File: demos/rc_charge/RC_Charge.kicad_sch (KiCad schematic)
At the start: 3 parts

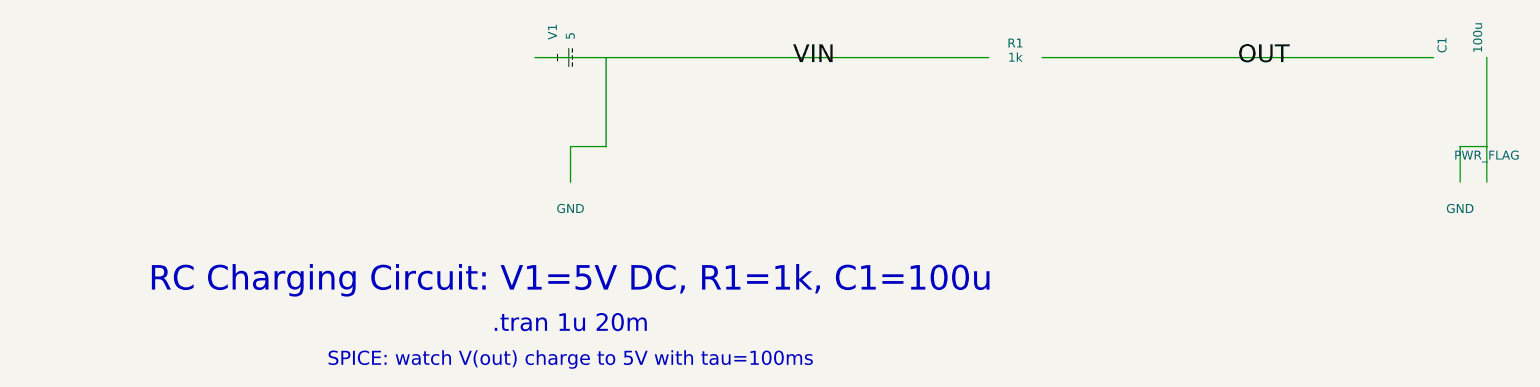
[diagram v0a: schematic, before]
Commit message: feat: Integrate SPICE simulation support into KiCad's GUI
- Added `handleSimulate` method in `api_handler_sch` to manage SPICE simulations.
- Implemented a new `Simulate` command in the API to trigger simulations from the schematic.
- Enhanced `NGSPICE` integration to handle optional symbols for compatibility with various builds.
- Introduced `kicad_sch_simulate_gui` function in Python client to run simulations and display results in KiCad's GUI.
- Updated tests to include simulation functionality and validate the integration.
- Documented changes and usage instructions for the new simulation features.
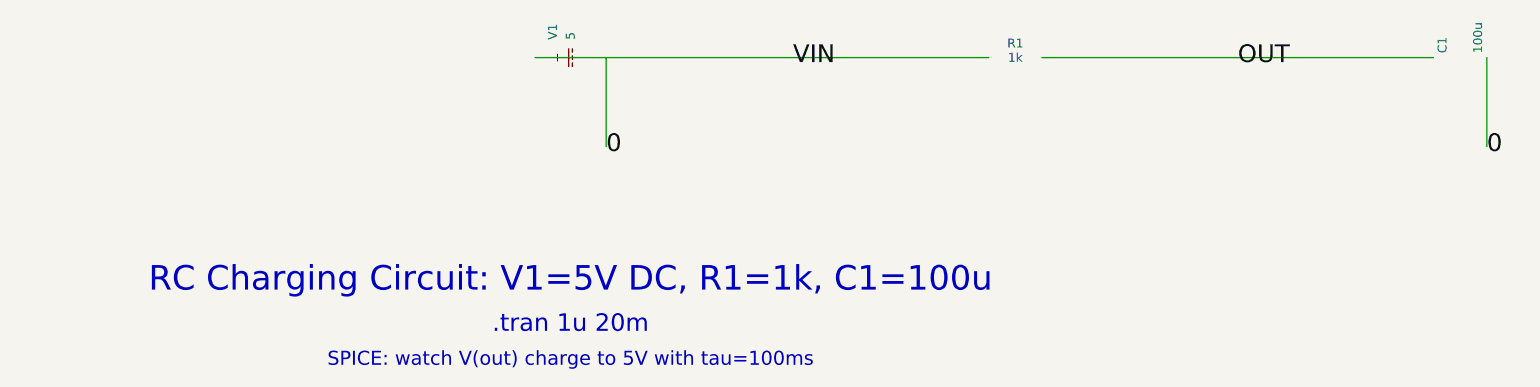
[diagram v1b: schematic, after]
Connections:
- net GND renamed 0

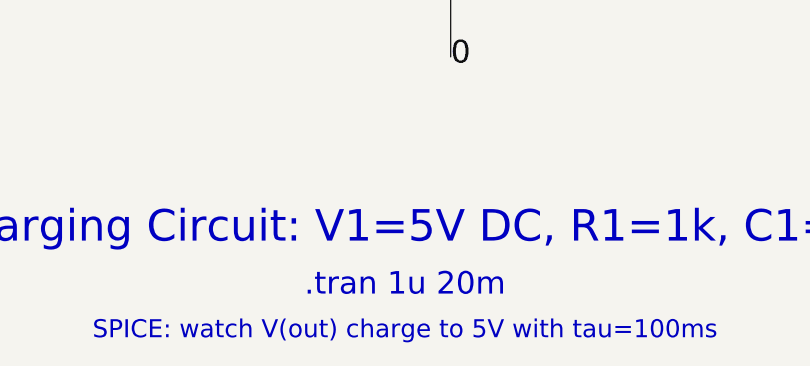
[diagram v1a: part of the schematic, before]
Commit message: feat: 增加信号自动显示功能，优化 SPICE 仿真结果分析
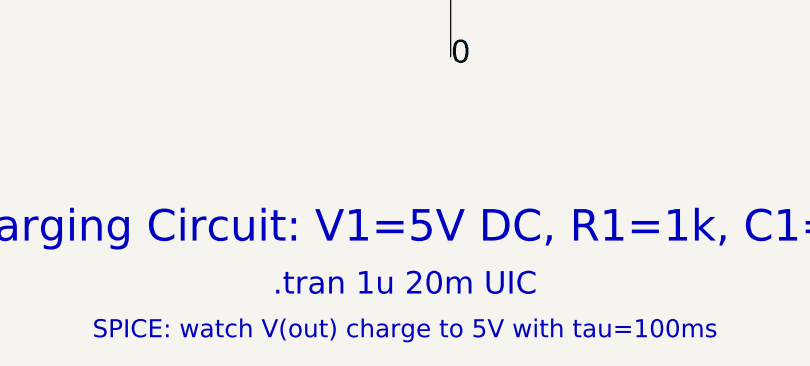
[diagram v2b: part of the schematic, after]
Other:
- note added: ".tran 1u 20m UIC"
- note removed: ".tran 1u 20m"
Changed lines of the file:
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@@
 		(title "RC Charging Circuit")
 	)
-	(text ".tran 1u 20m"
+	(text ".tran 1u 20m UIC"
 		(exclude_from_sim no)
 		(at 63.5 114.3 0)
@@
 		)
 	)
+	(text "SPICE: watch V(out) charge to 5V with tau=100ms"
+		(exclude_from_sim no)
+		(at 63.5 119.38 0)
+		(effects
+			(font
+				(size 2 2)
+			)
+		)
+	)
 	(text "RC Charging Circuit: V1=5V DC, R1=1k, C1=100u"
 		(exclude_from_sim no)
@@
 		)
 	)
-	(text "SPICE: watch V(out) charge to 5V with tau=100ms"
-		(exclude_from_sim no)
-		(at 63.5 119.38 0)
-		(effects
-			(font
-				(size 2 2)
-			)
+	(wire
+		(pts
+			(xy 130.81 76.2) (xy 186.69 76.2)
+		)
+		(stroke
+			(width 0)
+			(type default)
+		)
+	)
+	(wire
+		(pts
+			(xy 194.31 76.2) (xy 194.31 88.9)
+		)
+		(stroke
+			(width 0)
+			(type default)
 		)
 	)
@@
 	(wire
 		(pts
-			(xy 130.81 76.2) (xy 186.69 76.2)
+			(xy 68.58 76.2) (xy 68.58 88.9)
 		)
 		(stroke
@@
 		)
 	)
-	(wire
-		(pts
-			(xy 194.31 76.2) (xy 194.31 88.9)
-		)
-		(stroke
-			(width 0)
-			(type default)
-		)
-	)
-	(wire
-		(pts
-			(xy 68.58 76.2) (xy 68.58 88.9)
-		)
-		(stroke
-			(width 0)
-			(type default)
+	(label "VIN"
+		(at 95.25 76.2 0)
+		(effects
+			(font
+				(size 2.54 2.54)
+			)
 		)
 	)
@@
 		)
 	)
-	(label "VIN"
-		(at 95.25 76.2 0)
-		(effects
-			(font
-				(size 2.54 2.54)
-			)
-		)
-	)
 	(label "0"
 		(at 68.58 88.9 0)
@@
 			(font
 				(size 2.54 2.54)
+			)
+		)
+	)
+	(symbol
+		(lib_id "Device:C")
+		(at 190.5 76.2 90)
+		(unit 1)
+		(body_style 0)
+		(exclude_from_sim no)
+		(in_bom yes)
+		(on_board yes)
+		(in_pos_files yes)
+		(dnp no)
+		(property "Reference" "C1"
+			(at 187.96 75.565 0)
+			(show_name no)
+			(do_not_autoplace no)
+			(effects
+				(font
+					(size 1.27 1.27)
+				)
+				(justify left)
+			)
+		)
+		(property "Value" "100u"
+			(at 193.04 75.565 0)
+			(show_name no)
+			(do_not_autoplace no)
+			(effects
+				(font
+					(size 1.27 1.27)
+				)
+				(justify left)
+			)
+		)
+		(property "Footprint" ""
+			(at 194.31 75.2348 0)
+			(hide yes)
+			(show_name no)
+			(do_not_autoplace no)
+			(effects
+				(font
+					(size 1.27 1.27)
+				)
+			)
+		)
+		(property "Datasheet" ""
+			(at 190.5 76.2 0)
+			(hide yes)
+			(show_name no)
+			(do_not_autoplace no)
+			(effects
+				(font
+					(size 1.27 1.27)
+				)
+			)
+		)
+		(property "Description" "Unpolarized capacitor"
+			(at 190.5 76.2 0)
+			(hide yes)
+			(show_name no)
+			(do_not_autoplace no)
+			(effects
+				(font
+					(size 1.27 1.27)
+				)
+			)
+		)
+		(pin "2"
+		)
+		(pin "1"
+		)
+		(instances
+			(project "RC_Charge"
+				(path "/91a1d6ab-baa3-4e2f-aded-405b766975b0"
+					(reference "C1")
+					(unit 1)
+				)
 			)
 		)
@@
 	)
 	(symbol
-		(lib_id "Device:C")
-		(at 190.5 76.2 90)
-		(unit 1)
-		(body_style 0)
-		(exclude_from_sim no)
-		(in_bom yes)
-		(on_board yes)
-		(in_pos_files yes)
-		(dnp no)
-		(property "Reference" "C1"
-			(at 187.96 75.565 0)
-			(show_name no)
-			(do_not_autoplace no)
-			(effects
-				(font
-					(size 1.27 1.27)
-				)
-				(justify left)
-			)
-		)
-		(property "Value" "100u"
-			(at 193.04 75.565 0)
-			(show_name no)
-			(do_not_autoplace no)
-			(effects
-				(font
-					(size 1.27 1.27)
-				)
-				(justify left)
-			)
-		)
-		(property "Footprint" ""
-			(at 194.31 75.2348 0)
-			(hide yes)
-			(show_name no)
-			(do_not_autoplace no)
-			(effects
-				(font
-					(size 1.27 1.27)
-				)
-			)
-		)
-		(property "Datasheet" ""
-			(at 190.5 76.2 0)
-			(hide yes)
-			(show_name no)
-			(do_not_autoplace no)
-			(effects
-				(font
-					(size 1.27 1.27)
-				)
-			)
-		)
-		(property "Description" "Unpolarized capacitor"
-			(at 190.5 76.2 0)
-			(hide yes)
-			(show_name no)
-			(do_not_autoplace no)
-			(effects
-				(font
-					(size 1.27 1.27)
-				)
-			)
-		)
-		(pin "2"
-		)
-		(pin "1"
-		)
-		(instances
-			(project "RC_Charge"
-				(path "/91a1d6ab-baa3-4e2f-aded-405b766975b0"
-					(reference "C1")
-					(unit 1)
-				)
-			)
-		)
-	)
-	(symbol
 		(lib_id "Simulation_SPICE:VDC")
 		(at 63.5 76.2 90)
@@
 			)
 		)
+		(pin "1"
+		)
 		(pin "2"
 		)
-		(pin "1"
-		)
 		(instances
